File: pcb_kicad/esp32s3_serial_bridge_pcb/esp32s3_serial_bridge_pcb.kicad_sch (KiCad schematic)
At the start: 11 parts, among them J1 Conn_01x22_Socket, J2 Conn_01x22_Socket, J3 Conn_01x06_Socket, J4 Conn_01x06_Socket, J5 Conn_01x06_Socket, J6 Barrel_Jack_Switch, U2 R-78C5.0-1.0, U3 ESP32-S3-DevKitC-3rd-party-57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

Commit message: add PCB ESP32S3-Serial-Bridge V1.0 Kerberos
add PCB ESP32S3-Serial-Bridge V1.0 Kerberos
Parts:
- U3: value ESP32-S3-DevKitC-3rd-party-57x28 -> ESP32-S3-DevKitC-3rd-party-5715x2794; footprint PCM_Espressif:ESP32-S3-DevKitC_3rd_party_57x28 -> PCM_Espressif:ESP32-S3-DevKitC_3rd_party_5715x2794
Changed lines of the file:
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@@
 			)
 		)
-		(property "Value" "ESP32-S3-DevKitC-3rd-party-57x28"
+		(property "Value" "ESP32-S3-DevKitC-3rd-party-5715x2794"
 			(at 135.4933 139.7 0)
 			(effects
@@
 			)
 		)
-		(property "Footprint" "PCM_Espressif:ESP32-S3-DevKitC_3rd_party_57x28"
+		(property "Footprint" "PCM_Espressif:ESP32-S3-DevKitC_3rd_party_5715x2794"
 			(at 133.35 148.59 0)
 			(effects

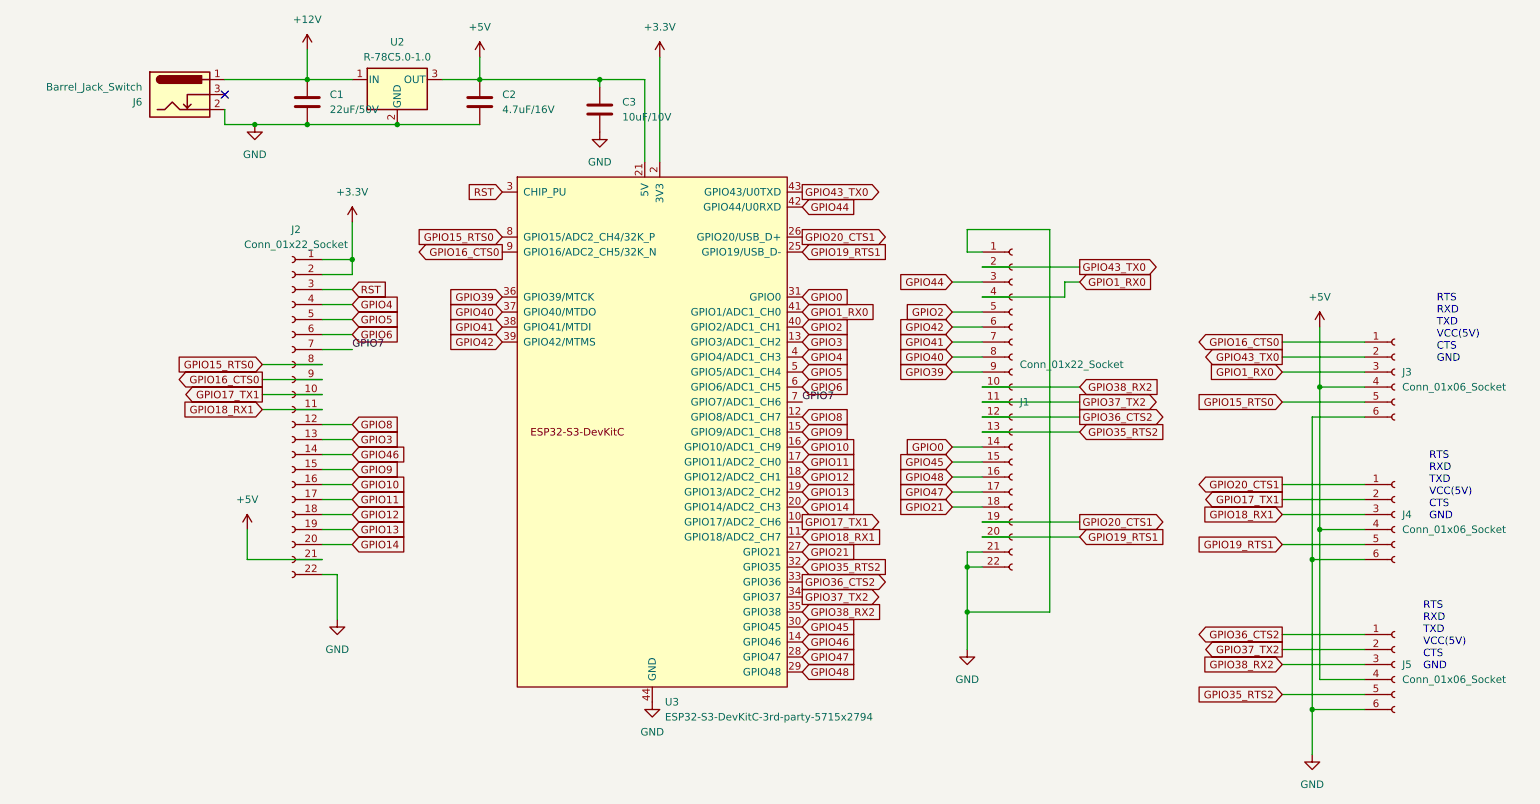
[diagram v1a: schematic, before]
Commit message: PCBもCTS: GPIO20 -> 10, RTS: GPIO19 -> 9 に変更
PCBもCTS: GPIO20 -> 10, RTS: GPIO19 -> 9 に変更
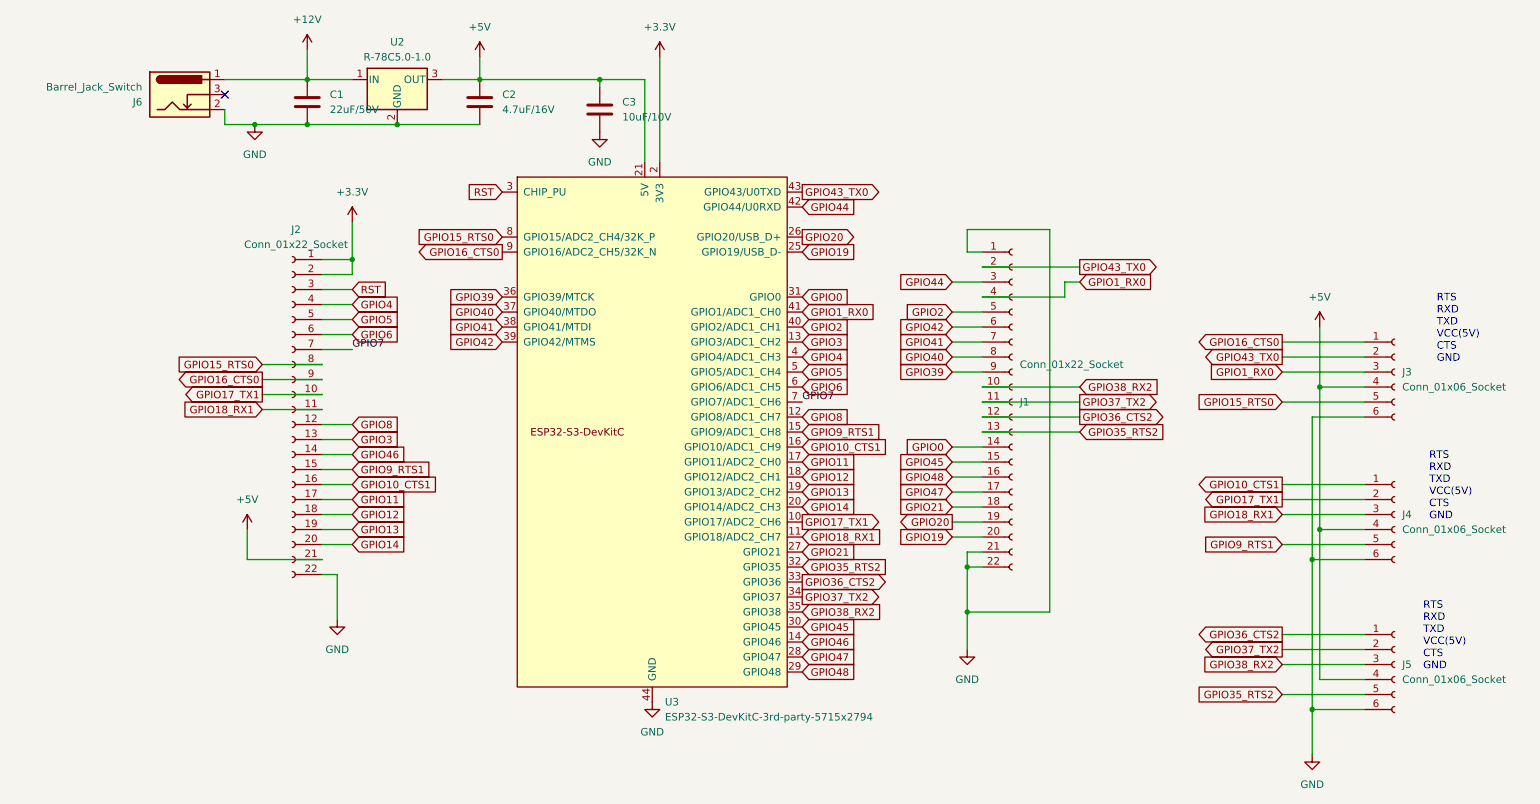
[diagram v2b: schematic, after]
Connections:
- net GPIO10 renamed GPIO10_CTS1
- net GPIO10_CTS1: now also J4.1 (Pin_1)
- net GPIO19_RTS1 renamed GPIO19
- net GPIO19: no longer J4.5 (Pin_5)
- net GPIO20_CTS1 renamed GPIO20
- net GPIO20: no longer J4.1 (Pin_1)
- net GPIO9 renamed GPIO9_RTS1
- net GPIO9_RTS1: now also J4.5 (Pin_5)
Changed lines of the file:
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@@
 	(title_block
 		(title "ESP32S3-Serial-Bridge")
-		(date "2026-01-27")
-		(rev "V1.0")
+		(date "2026-02-25")
+		(rev "V1.1")
 		(company "takurx")
+		(comment 1 "CTS: GPIO20 -> 10, RTS: GPIO19 -> 9 に変更")
 	)
 	(text "RTS\nRXD\nTXD\nVCC(5V)\nCTS\nGND"
@@
 	(wire
 		(pts
-			(xy 189.23 106.68) (xy 205.74 106.68)
-		)
-		(stroke
-			(width 0)
-			(type default)
-		)
-	)
-	(wire
-		(pts
 			(xy 189.23 83.82) (xy 205.74 83.82)
 		)
@@
 	(wire
 		(pts
+			(xy 184.15 109.22) (xy 189.23 109.22)
+		)
+		(stroke
+			(width 0)
+			(type default)
+		)
+	)
+	(wire
+		(pts
 			(xy 246.38 83.82) (xy 246.38 73.66)
 		)
@@
 	(wire
 		(pts
-			(xy 189.23 109.22) (xy 205.74 109.22)
-		)
-		(stroke
-			(width 0)
-			(type default)
-		)
-	)
-	(wire
-		(pts
 			(xy 77.47 64.77) (xy 82.55 64.77)
 		)
@@
 	(wire
 		(pts
+			(xy 184.15 106.68) (xy 189.23 106.68)
+		)
+		(stroke
+			(width 0)
+			(type default)
+		)
+	)
+	(wire
+		(pts
 			(xy 186.69 121.92) (xy 186.69 128.27)
 		)
@@
 		)
 	)
-	(global_label "GPIO19_RTS1"
+	(global_label "GPIO19"
 		(shape input)
 		(at 158.75 60.96 0)
@@
 		)
 		(property "Intersheetrefs" "${INTERSHEET_REFS}"
-			(at 174.2537 60.96 0)
+			(at 168.6295 60.96 0)
 			(effects
 				(font
@@
 		)
 	)
-	(global_label "GPIO20_CTS1"
+	(global_label "GPIO10_CTS1"
 		(shape output)
 		(at 240.03 100.33 180)
@@
 		)
 	)
-	(global_label "GPIO10"
+	(global_label "GPIO10_CTS1"
 		(shape input)
 		(at 82.55 100.33 0)
@@
 		)
 		(property "Intersheetrefs" "${INTERSHEET_REFS}"
-			(at 92.4295 100.33 0)
+			(at 98.0537 100.33 0)
 			(effects
 				(font
@@
 		)
 	)
-	(global_label "GPIO9"
+	(global_label "GPIO9_RTS1"
 		(shape input)
 		(at 82.55 97.79 0)
@@
 		)
 		(property "Intersheetrefs" "${INTERSHEET_REFS}"
-			(at 91.22 97.79 0)
+			(at 96.8442 97.79 0)
 			(effects
 				(font
@@
 		)
 	)
-	(global_label "GPIO10"
+	(global_label "GPIO10_CTS1"
 		(shape input)
 		(at 158.75 93.98 0)
@@
 		)
 		(property "Intersheetrefs" "${INTERSHEET_REFS}"
-			(at 168.6295 93.98 0)
+			(at 174.2537 93.98 0)
 			(effects
 				(font
@@
 		)
 	)
-	(global_label "GPIO19_RTS1"
+	(global_label "GPIO9_RTS1"
 		(shape input)
 		(at 240.03 110.49 180)
@@
 		)
 		(property "Intersheetrefs" "${INTERSHEET_REFS}"
-			(at 224.5263 110.49 0)
+			(at 225.7358 110.49 0)
 			(effects
 				(font
@@
 		)
 	)
-	(global_label "GPIO20_CTS1"
+	(global_label "GPIO20"
 		(shape output)
-		(at 205.74 106.68 0)
+		(at 184.15 106.68 180)
 		(fields_autoplaced yes)
 		(effects
@@
 				(size 1.27 1.27)
 			)
-			(justify left)
+			(justify right)
 		)
 		(property "Intersheetrefs" "${INTERSHEET_REFS}"
-			(at 221.2437 106.68 0)
+			(at 174.2705 106.68 0)
 			(effects
 				(font
 					(size 1.27 1.27)
 				)
-				(justify left)
+				(justify right)
 				(hide yes)
 			)
@@
 		)
 	)
-	(global_label "GPIO19_RTS1"
+	(global_label "GPIO19"
 		(shape input)
-		(at 205.74 109.22 0)
+		(at 184.15 109.22 180)
 		(fields_autoplaced yes)
 		(effects
@@
 				(size 1.27 1.27)
 			)
-			(justify left)
+			(justify right)
 		)
 		(property "Intersheetrefs" "${INTERSHEET_REFS}"
-			(at 221.2437 109.22 0)
+			(at 174.2705 109.22 0)
 			(effects
 				(font
 					(size 1.27 1.27)
 				)
-				(justify left)
+				(justify right)
 				(hide yes)
 			)
@@
 		)
 	)
-	(global_label "GPIO9"
+	(global_label "GPIO9_RTS1"
 		(shape input)
 		(at 158.75 91.44 0)
@@
 		)
 		(property "Intersheetrefs" "${INTERSHEET_REFS}"
-			(at 167.42 91.44 0)
+			(at 173.0442 91.44 0)
 			(effects
 				(font
@@
 		)
 	)
-	(global_label "GPIO20_CTS1"
+	(global_label "GPIO20"
 		(shape output)
 		(at 158.75 58.42 0)
@@
 		)
 		(property "Intersheetrefs" "${INTERSHEET_REFS}"
-			(at 174.2537 58.42 0)
+			(at 168.6295 58.42 0)
 			(effects
 				(font
